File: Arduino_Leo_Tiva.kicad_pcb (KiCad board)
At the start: 4 copper layers, 68.6 x 52.1 mm, 53 parts, among them J1 USB_OTG, J10 Digital, J11 TDI, J12 TDO, J13 TXD, J14 RXD, J15 -AREF, J16 +AREF, J17 SPI 2 (D6,D7), J18 SERIAL 3, 4, J19 SERIAL 2, J2 TCK, J20 SPI 0, J21 SERIAL 1, J3 RST, J4 PF4, J5 ~HIB, J5V1 +5V, J6 TMS, J7 Power, J8 Analog, J9 Digital, SW1 RESET, U1 TM4C123GH6PM, U2 LM1117IMPX-3.3, Y1 32.768Khz, Y2 16MHz

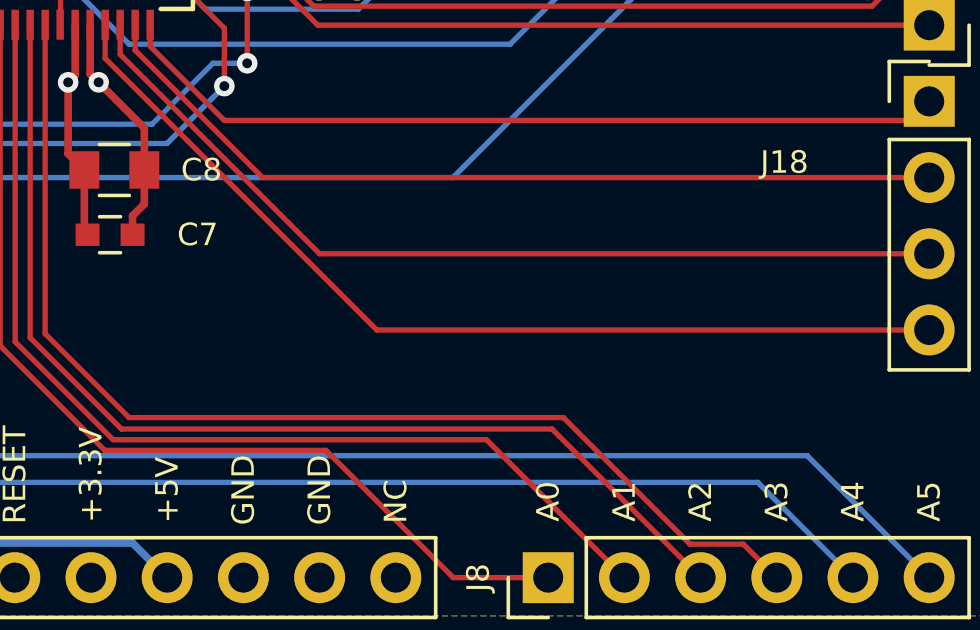
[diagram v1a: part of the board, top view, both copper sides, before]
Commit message: Added KiCAD silkscreen and name to top layer
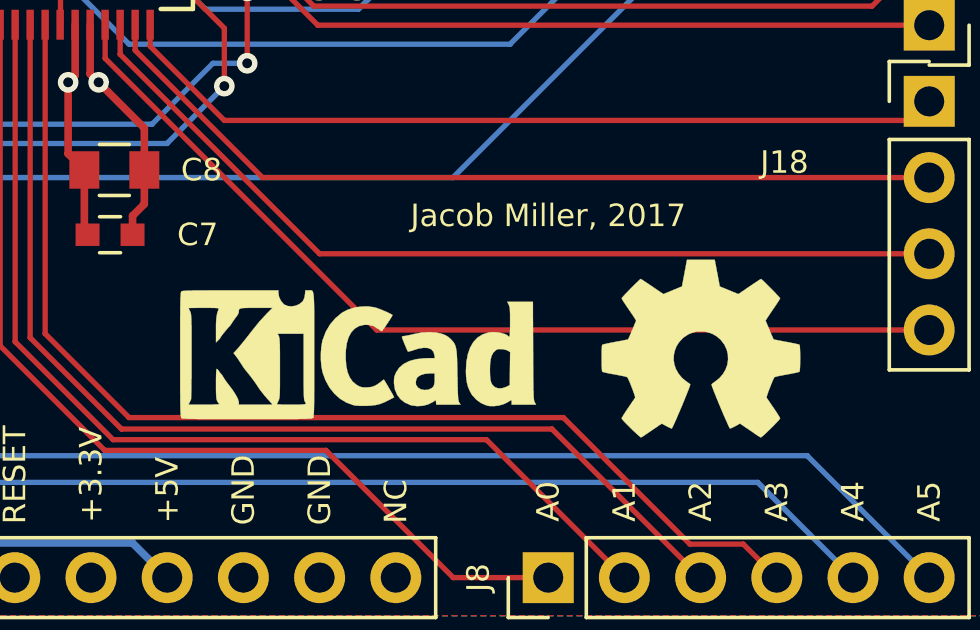
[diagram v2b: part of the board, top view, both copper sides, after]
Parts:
- added REF**: KiCAD Logo, Symbols:Symbol_KiCAD-Logo_CopperAndSilkScreenTop, F.Cu at (155.4, 116.2)
- added REF***: OSHW-Symbol_6.7x6mm_SilkScreen, Symbols:OSHW-Symbol_6.7x6mm_SilkScreen, F.Cu at (166.9, 116.2)
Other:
- board text added: "Jacob Miller, 2017"

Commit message: Fixed issue with incorrect schematic symbol and footprint for 3.3V regulator IC. Fixed typo in path
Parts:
- removed M** (x2): Lego-Hole-4.8mm, Custon-Mounting-Holes:Lego-Hole
- removed REF**: KiCAD Logo, Symbols:Symbol_KiCAD-Logo_CopperAndSilkScreenTop
- removed REF***: OSHW-Symbol_6.7x6mm_SilkScreen, Symbols:OSHW-Symbol_6.7x6mm_SilkScreen
- U2: value LM1117IMPX-3.3 -> LM1117-3.3; footprint TO_SOT_Packages_SMD_Local:SOT-223-3Lead_TabPin2 -> TO_SOT_Packages_SMD_Local:SOT-223
- turned U2 to 180 degrees
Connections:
- U2 pad 1: +5V -> GNDREF
- U2 pad 2: GNDREF -> +3V3
- U2 pad 3: +3V3 -> +5V
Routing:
- net GNDREF: track 92.7 -> 79.1 mm
- net +3V3: track 46.6 -> 52.0 mm
- net +5V: track 90.1 -> 92.2 mm
- net /PB6(MISO): track 19.6 -> 20.3 mm

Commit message: Fixed "Swap UART Labels on D0,D1 #7"
Had U0Tx and U0Rx labled incorrectly in schematic.
Fixed labels and rerouted signals to correct pins.
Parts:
- J3: value RST -> ~RST
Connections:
- U1 pad 17: /1(Tx) -> /0(Rx)
- U1 pad 18: /0(Rx) -> /1(Tx)
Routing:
- net /0(Rx): track 75.8 -> 71.6 mm, vias 2 -> 1
- net /PD7(U2TX): track 39.6 -> 42.3 mm, vias 2 -> 3
- net /1(Tx): track 68.5 -> 69.4 mm, vias 2 -> 1

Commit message: Modified LEGO mounting hole - Increased width by 0.05 mm - Removed through hole plating (now NPTH)
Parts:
- added P1: LEGO_Hole, Custom-Mounting-Holes:Lego-Hole, F.Cu at (116.0, 79.1)
- added P2: LEGO_Hole, Custom-Mounting-Holes:Lego-Hole, F.Cu at (116.0, 119.1)
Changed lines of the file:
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@@
   (general
     (links 134)
-    (no_connects 3)
+    (no_connects 1)
     (area 110.922999 73.584999 179.653001 125.805001)
     (thickness 1.6)
@@
     (tracks 631)
     (zones 0)
-    (modules 51)
+    (modules 53)
     (nets 59)
   )
@@
     )
   )
+  (module Custom-Mounting-Holes:Lego-Hole (layer Top)
+    (at 115.998 79.0956 90)
+    (tags "Lego, Hole")
+    (fp_text reference P1 (at 0 4 90) (layer F.SilkS)
+      (effects (font (size 0.75 0.75) (thickness 0.15)))
+    )
+    (fp_text value LEGO_Hole (at 0 -4 90) (layer F.Fab)
+      (effects (font (size 0.75 0.75) (thickness 0.15)))
+    )
+    (fp_line (start -4 -4) (end -3 -4) (layer Dwgs.User) (width 0.15))
+    (fp_line (start -4 -3) (end -4 -4) (layer Dwgs.User) (width 0.15))
+    (fp_line (start 4 4) (end 4 3) (layer Dwgs.User) (width 0.15))
+    (fp_line (start 3 4) (end 4 4) (layer Dwgs.User) (width 0.15))
+    (fp_line (start -4 4) (end -3 4) (layer Dwgs.User) (width 0.15))
+    (fp_line (start -4 3) (end -4 4) (layer Dwgs.User) (width 0.15))
+    (fp_line (start 4 -4) (end 3 -4) (layer Dwgs.User) (width 0.15))
+    (fp_line (start 4 -3) (end 4 -4) (layer Dwgs.User) (width 0.15))
+    (pad "" np_thru_hole circle (at 0 0 90) (size 6.05 6.05) (drill 4.8) (layers *.Cu *.Mask))
+  )
+  (module Custom-Mounting-Holes:Lego-Hole (layer Top)
+    (at 115.998 119.095 90)
+    (tags "Lego, Hole")
+    (fp_text reference P2 (at 0 4 90) (layer F.SilkS)
+      (effects (font (size 0.75 0.75) (thickness 0.15)))
+    )
+    (fp_text value LEGO_Hole (at 0 -4 90) (layer F.Fab)
+      (effects (font (size 0.75 0.75) (thickness 0.15)))
+    )
+    (fp_line (start -4 -4) (end -3 -4) (layer Dwgs.User) (width 0.15))
+    (fp_line (start -4 -3) (end -4 -4) (layer Dwgs.User) (width 0.15))
+    (fp_line (start 4 4) (end 4 3) (layer Dwgs.User) (width 0.15))
+    (fp_line (start 3 4) (end 4 4) (layer Dwgs.User) (width 0.15))
+    (fp_line (start -4 4) (end -3 4) (layer Dwgs.User) (width 0.15))
+    (fp_line (start -4 3) (end -4 4) (layer Dwgs.User) (width 0.15))
+    (fp_line (start 4 -4) (end 3 -4) (layer Dwgs.User) (width 0.15))
+    (fp_line (start 4 -3) (end 4 -4) (layer Dwgs.User) (width 0.15))
+    (pad "" np_thru_hole circle (at 0 0 90) (size 6.05 6.05) (drill 4.8) (layers *.Cu *.Mask))
+  )
   (gr_text "Jacob Miller, 2017" (at 161.798 111.76) (layer F.SilkS)

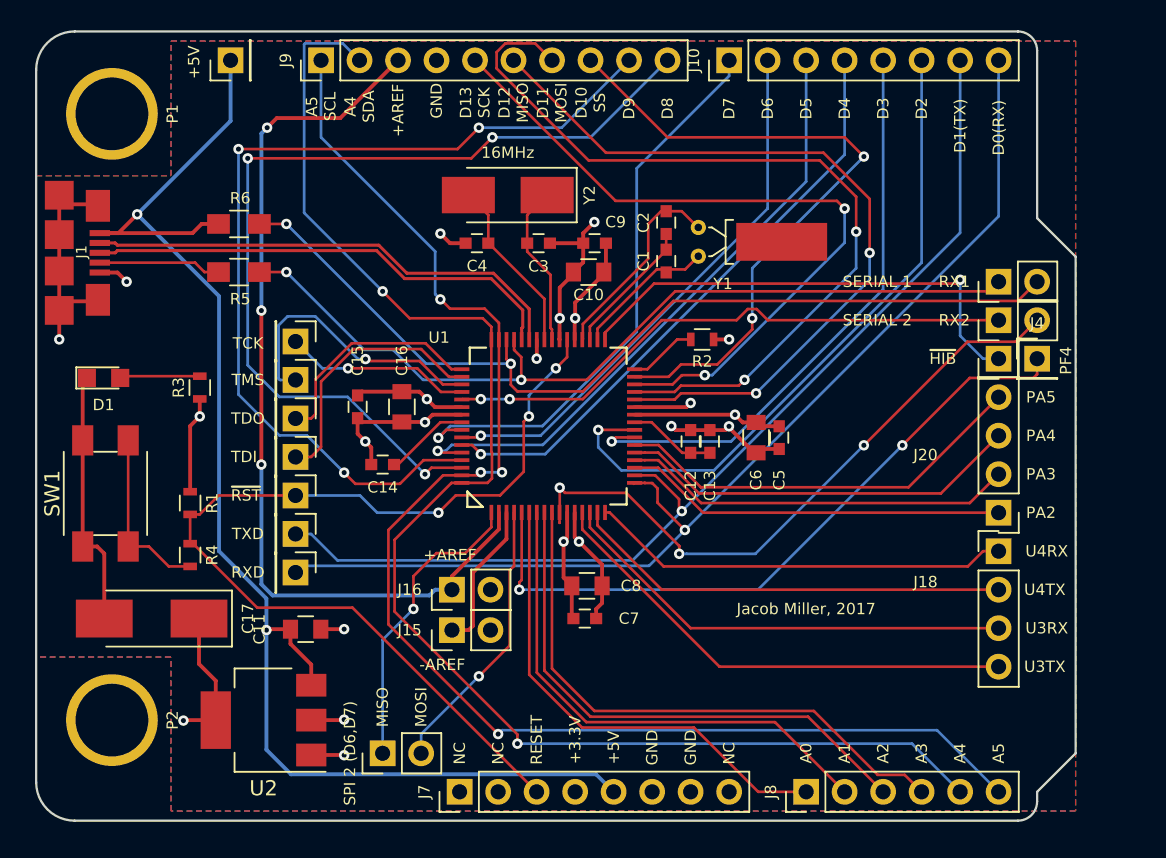
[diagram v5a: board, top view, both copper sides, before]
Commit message: Major changes to board layout and design leading towards revisoin v1.1
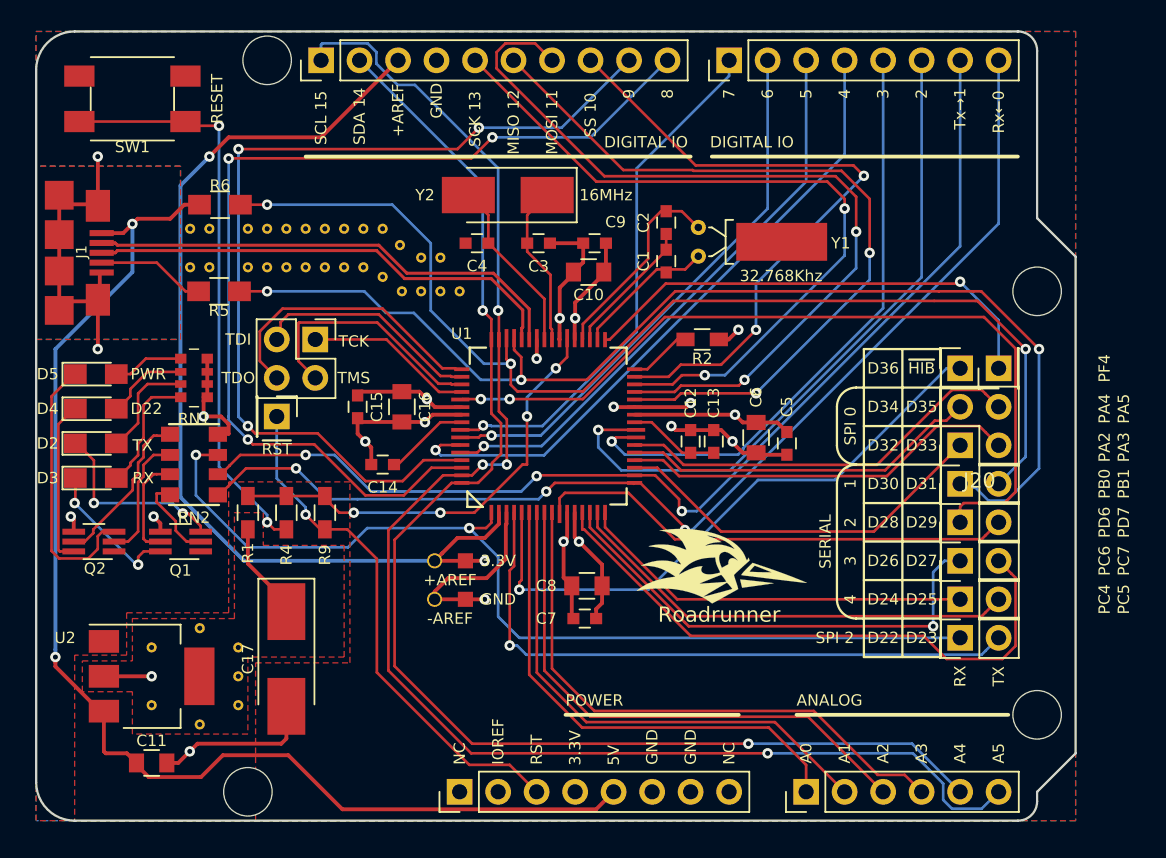
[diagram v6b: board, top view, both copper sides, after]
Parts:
- removed D1: Green, LEDs:LED_0805
- removed J11: TDI, Pin_Headers:Pin_Header_Straight_1x01_Pitch2.54mm
- removed J12: TDO, Pin_Headers:Pin_Header_Straight_1x01_Pitch2.54mm
- removed J18: SERIAL 3, 4, Socket_Strips:Socket_Strip_Straight_1x04_Pitch2.54mm
- removed J5V1: +5V, Pin_Headers:Pin_Header_Straight_1x01_Pitch2.54mm
- removed J6: TMS, Pin_Headers:Pin_Header_Straight_1x01_Pitch2.54mm
- removed P1, P2: LEGO_Hole, Custom-Mounting-Holes:Lego-Hole
- removed R3: 75, Resistors_SMD:R_0603
- added D2: Green, LEDs:LED_0805_HandSoldering, F.Cu at (114.9, 100.8)
- added D3: Green, LEDs:LED_0805_HandSoldering, F.Cu at (114.9, 103.1)
- added D4: Green, LEDs:LED_0805_HandSoldering, F.Cu at (114.9, 98.6)
- added D5: Green, LEDs:LED_0805_HandSoldering, F.Cu at (114.9, 96.3)
- added G***: LOGO, Custom-Mounting-Holes:My_Roadrunner, B.Cu at (123.7, 99.7)
- added G***: LOGO, Custom-Mounting-Holes:My_Roadrunner_smaller, F.Cu at (156.5, 109.0)
- added Q1: UM6K33N, TO_SOT_Packages_SMD_Local:SOT-363_SC-70-6_Handsoldering, F.Cu at (120.5, 107.3)
- added Q2: UM6K33N, TO_SOT_Packages_SMD_Local:SOT-363_SC-70-6_Handsoldering, F.Cu at (114.8, 107.3)
- added R9: 10k, Resistors_SMD:R_0603_HandSoldering, F.Cu at (130.0, 105.4)
- added REF**: VIA-0.33mm, Custom-Mounting-Holes:VIA-0.33mm, F.Cu at (124.3, 116.2)
- added REF**: VIA-0.33mm, Custom-Mounting-Holes:VIA-0.33mm, F.Cu at (121.2, 86.7)
- added REF**: VIA-0.33mm, Custom-Mounting-Holes:VIA-0.33mm, F.Cu at (122.4, 86.7)
- added REF**: VIA-0.33mm, Custom-Mounting-Holes:VIA-0.33mm, F.Cu at (125.0, 86.7)
- added REF**: VIA-0.33mm, Custom-Mounting-Holes:VIA-0.33mm, F.Cu at (126.2, 86.7)
- added REF**: VIA-0.33mm, Custom-Mounting-Holes:VIA-0.33mm, F.Cu at (127.5, 86.7)
- added REF**: VIA-0.33mm, Custom-Mounting-Holes:VIA-0.33mm, F.Cu at (125.0, 89.2)
- added REF**: VIA-0.33mm, Custom-Mounting-Holes:VIA-0.33mm, F.Cu at (126.2, 89.2)
- added REF**: VIA-0.33mm, Custom-Mounting-Holes:VIA-0.33mm, F.Cu at (127.5, 89.2)
- added REF**: VIA-0.33mm, Custom-Mounting-Holes:VIA-0.33mm, F.Cu at (128.8, 86.7)
- added REF**: VIA-0.33mm, Custom-Mounting-Holes:VIA-0.33mm, F.Cu at (128.8, 89.2)
- added REF**: VIA-0.33mm, Custom-Mounting-Holes:VIA-0.33mm, F.Cu at (124.3, 118.1)
- added REF**: VIA-0.33mm, Custom-Mounting-Holes:VIA-0.33mm, F.Cu at (130.0, 89.2)
- added REF**: VIA-0.33mm, Custom-Mounting-Holes:VIA-0.33mm, F.Cu at (131.3, 89.2)
- added REF**: VIA-0.33mm, Custom-Mounting-Holes:VIA-0.33mm, F.Cu at (138.9, 90.8)
- added REF**: VIA-0.33mm, Custom-Mounting-Holes:VIA-0.33mm, F.Cu at (137.7, 90.8)
- added REF**: VIA-0.33mm, Custom-Mounting-Holes:VIA-0.33mm, F.Cu at (136.4, 90.8)
- added REF**: VIA-0.33mm, Custom-Mounting-Holes:VIA-0.33mm, F.Cu at (135.1, 90.8)
- added REF**: VIA-0.33mm, Custom-Mounting-Holes:VIA-0.33mm, F.Cu at (133.9, 89.9)
- added REF**: VIA-0.33mm, Custom-Mounting-Holes:VIA-0.33mm, F.Cu at (132.6, 89.2)
- added REF**: VIA-0.33mm, Custom-Mounting-Holes:VIA-0.33mm, F.Cu at (137.7, 88.6)
- added REF**: VIA-0.33mm, Custom-Mounting-Holes:VIA-0.33mm, F.Cu at (136.4, 88.6)
- added REF**: VIA-0.33mm, Custom-Mounting-Holes:VIA-0.33mm, F.Cu at (124.3, 114.3)
- added REF**: VIA-0.33mm, Custom-Mounting-Holes:VIA-0.33mm, F.Cu at (135.0, 87.8)
- added REF**: VIA-0.33mm, Custom-Mounting-Holes:VIA-0.33mm, F.Cu at (133.9, 86.7)
- added REF**: VIA-0.33mm, Custom-Mounting-Holes:VIA-0.33mm, F.Cu at (132.6, 86.7)
- added REF**: VIA-0.33mm, Custom-Mounting-Holes:VIA-0.33mm, F.Cu at (131.3, 86.7)
- added REF**: VIA-0.33mm, Custom-Mounting-Holes:VIA-0.33mm, F.Cu at (130.0, 86.7)
- added REF**: VIA-0.33mm, Custom-Mounting-Holes:VIA-0.33mm, F.Cu at (121.8, 119.4)
- added REF**: VIA-0.33mm, Custom-Mounting-Holes:VIA-0.33mm, F.Cu at (121.8, 113.0)
- added REF**: VIA-0.33mm, Custom-Mounting-Holes:VIA-0.33mm, F.Cu at (118.6, 118.1)
- added REF**: VIA-0.33mm, Custom-Mounting-Holes:VIA-0.33mm, F.Cu at (118.6, 114.3)
- added REF**: VIA-0.33mm, Custom-Mounting-Holes:VIA-0.33mm, F.Cu at (122.4, 89.2)
- added REF**: VIA-0.33mm, Custom-Mounting-Holes:VIA-0.33mm, F.Cu at (121.2, 89.2)
- added REF***: KiCad-Logo2_12mm_SilkScreen, Symbols:KiCad-Logo2_12mm_SilkScreen, B.Cu at (164.3, 99.7)
- added REF***: OSHW-Logo2_9.8x8mm_SilkScreen, Symbols:OSHW-Logo2_9.8x8mm_SilkScreen, B.Cu at (144.8, 99.7)
- added RN1: 75, Project-Symbols_Local:YC164-JR-0775RL, F.Cu at (121.4, 96.5)
- added RN2: 10k, Project-Symbols_Local:CRA12E08310K0JTR, F.Cu at (121.4, 102.2)
- added T1: M_Hole, Custom-Mounting-Holes:ArduinoMountingHole_3.2mm, F.Cu at (125.0, 123.8)
- added T2: M_Hole, Custom-Mounting-Holes:ArduinoMountingHole_3.2mm, F.Cu at (177.0, 118.7)
- added T3: M_Hole, Custom-Mounting-Holes:ArduinoMountingHole_3.2mm, F.Cu at (126.2, 75.6)
- added T4: M_Hole, Custom-Mounting-Holes:ArduinoMountingHole_3.2mm, F.Cu at (177.0, 90.8)
- J13: value TXD -> SERIAL 4; footprint Pin_Headers:Pin_Header_Straight_1x01_Pitch2.54mm -> Socket_Strips:Socket_Strip_Straight_1x02_Pitch2.54mm
- J14: value RXD -> SERIAL 3; footprint Pin_Headers:Pin_Header_Straight_1x01_Pitch2.54mm -> Socket_Strips:Socket_Strip_Straight_1x02_Pitch2.54mm
- J15, J16: footprint Pin_Headers:Pin_Header_Straight_1x02_Pitch2.54mm -> Custom-Mounting-Holes:NetTie-I_Connected_SMD
- J17: value SPI 2 (D6,D7) -> SPI 2 (D22,D23)
- J2: value TCK -> JTAG; footprint Pin_Headers:Pin_Header_Straight_1x01_Pitch2.54mm -> Connectors_Local:Pin_Header_Straight_2x02_Pitch2.54mm
- J20: footprint Socket_Strips:Socket_Strip_Straight_1x04_Pitch2.54mm -> Socket_Strips:Socket_Strip_Straight_2x02_Pitch2.54mm
- J5: footprint Pin_Headers:Pin_Header_Straight_1x01_Pitch2.54mm -> Socket_Strips:Socket_Strip_Straight_1x01_Pitch2.54mm
- R1, R2, R4: footprint Resistors_SMD:R_0603 -> Resistors_SMD:R_0603_HandSoldering
- moved J13 44.1 mm to (172.0, 111.1), turned to 90 degrees
- moved J14 43.9 mm to (172.0, 108.6), turned to 90 degrees
- moved J17 38.9 mm to (172.0, 113.7)
- moved SW1 26.1 mm to (117.3, 78.1), turned to 0 degrees
- moved J19 13.6 mm to (172.0, 106.0)
- moved J21 13.6 mm to (172.0, 103.5)
- moved C11 13.5 mm to (118.6, 121.9)
- moved C17 9.28 mm to (127.5, 115.1), turned to 270 degrees
- moved U2 7.93 mm to (118.6, 116.2), turned to 0 degrees
- moved R4 6.94 mm to (127.5, 105.4)
- moved J3 5.36 mm to (126.9, 99.1)
- moved J4 5.12 mm to (172.0, 95.9)
- moved J20 5.12 mm to (172.0, 101.0)
- moved R1 3.86 mm to (125.0, 105.4), turned to 90 degrees
- moved J15 2.04 mm to (138.3, 111.1), turned to 0 degrees
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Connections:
- J10 pad 7: /1(Tx) -> /D1(TX)
- J10 pad 8: /0(Rx) -> /D0(RX)
- J13 pad 1: /1(Tx) -> /PC4(U4RX)
- J14 pad 1: /0(Rx) -> /PC6(U3RX)
- J3 pad 1: /RESET -> /~RST
- J7 pad 2: (no net) -> +3V3
- J7 pad 3: /RESET -> /~RST
- R1 pad 2: /RESET -> /~TARGET_RST
- R4 pad 1: /RESET -> /~TARGET_RST
- U1 pad 17: /0(Rx) -> /D0(RX)
- U1 pad 18: /1(Tx) -> /D1(TX)
- U1 pad 38: /RESET -> /~TARGET_RST
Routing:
- net /D0(RX): track 0.00 -> 74.1 mm, vias 0 -> 3
- net /D1(TX): track 0.00 -> 71.8 mm, vias 0 -> 3
- net /0(Rx): track 71.6 -> 0.00 mm, vias 1 -> 0
- net /1(Tx): track 69.4 -> 0.00 mm, vias 1 -> 0
- net /RESET: track 65.6 -> 0.00 mm, vias 3 -> 0
- net /PB6(MISO): track 20.3 -> 64.4 mm, vias 1 -> 2
- net /~RST: track 0.00 -> 34.7 mm, vias 0 -> 1
- net /~TARGET_RST: track 0.00 -> 29.7 mm, vias 0 -> 4
- net Net-(R4-Pad2): track 11.6 -> 38.6 mm, vias 0 -> 2
- net /PB7(MOSI): track 18.4 -> 41.9 mm
- net /PB0(U1RX): track 57.2 -> 76.4 mm, vias 2 -> 3
- net /Q2D2: track 0.00 -> 17.9 mm
- net /PD6(U2RX): track 38.2 -> 54.2 mm
- net /PB1(U1TX): track 61.4 -> 75.4 mm, vias 2 -> 3
- net /Q1D2: track 0.00 -> 12.6 mm, vias 0 -> 2
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- added copper zone on F.Cu, net +3V3
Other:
- board text added: "1"
- board text added: "2"
- board text added: "3"
- board text added: "3.3V"
- board text added: "4"
- board text added: "5"
- board text added: "5V"
- board text added: "6"
- board text added: "7"
- board text added: "8"
- board text added: "9"
- board text added: "ANALOG"
- board text added: "D22"
- board text added: "D23"
- board text added: "D24"
- board text added: "D25"
- board text added: "D26"
- board text added: "D27"
- board text added: "D28"
- board text added: "D29"
- board text added: "D30"
- board text added: "D31"
- board text added: "D32"
- board text added: "D33"
- board text added: "D34"
- board text added: "D35"
- board text added: "D36"
- board text added: "DIGITAL IO"
- board text added: "IOREF"
- board text added: "MISO 12"
- board text added: "MOSI 11"
- board text added: "PB0"
- board text added: "PB1"
- board text added: "PC4"
- board text added: "PC5"
- board text added: "PC6"
- board text added: "PC7"
- board text added: "PD6"
- board text added: "PD7"
- board text added: "PF4"
- board text added: "POWER"
- board text added: "PWR"
- board text added: "RST"
- board text added: "RX"
- board text added: "Roadrunner"
- board text added: "Roadrunner Rev 1.1 (Jacob Miller 2017)"
- board text added: "Rx←0"
- board text added: "SCK 13"
- board text added: "SCL 15"
- board text added: "SDA 14"
- board text added: "SERIAL"
- board text added: "SPI 0"
- board text added: "SPI 2"
- board text added: "SS 10"
- board text added: "TCK"
- board text added: "TDI"
- board text added: "TDO"
- board text added: "TMS"
- board text added: "TX"
- board text added: "Tx→1"
- board text added: "~HIB"
- board text removed: "+3.3V"
- board text removed: "+5V"
- board text removed: "A4 SDA"
- board text removed: "A5 SCL"
- board text removed: "D0(RX)"
- board text removed: "D1(TX)"
- board text removed: "D10 SS"
- board text removed: "D11 MOSI"
- board text removed: "D12 MISO"
- board text removed: "D13 SCK"
- board text removed: "D2"
- board text removed: "D3"
- board text removed: "D4"
- board text removed: "D5"
- board text removed: "D6"
- board text removed: "D7"
- board text removed: "D8"
- board text removed: "D9"
- board text removed: "Jacob Miller, 2017"
- board text removed: "MISO"
- board text removed: "MOSI"
- board text removed: "RESET"
- board text removed: "U3RX"
- board text removed: "U3TX"
- board text removed: "U4RX"
- board text removed: "U4TX"

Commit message: Recent modifications to layout. Switching to resistor arrays. Adding Roadrunner image.
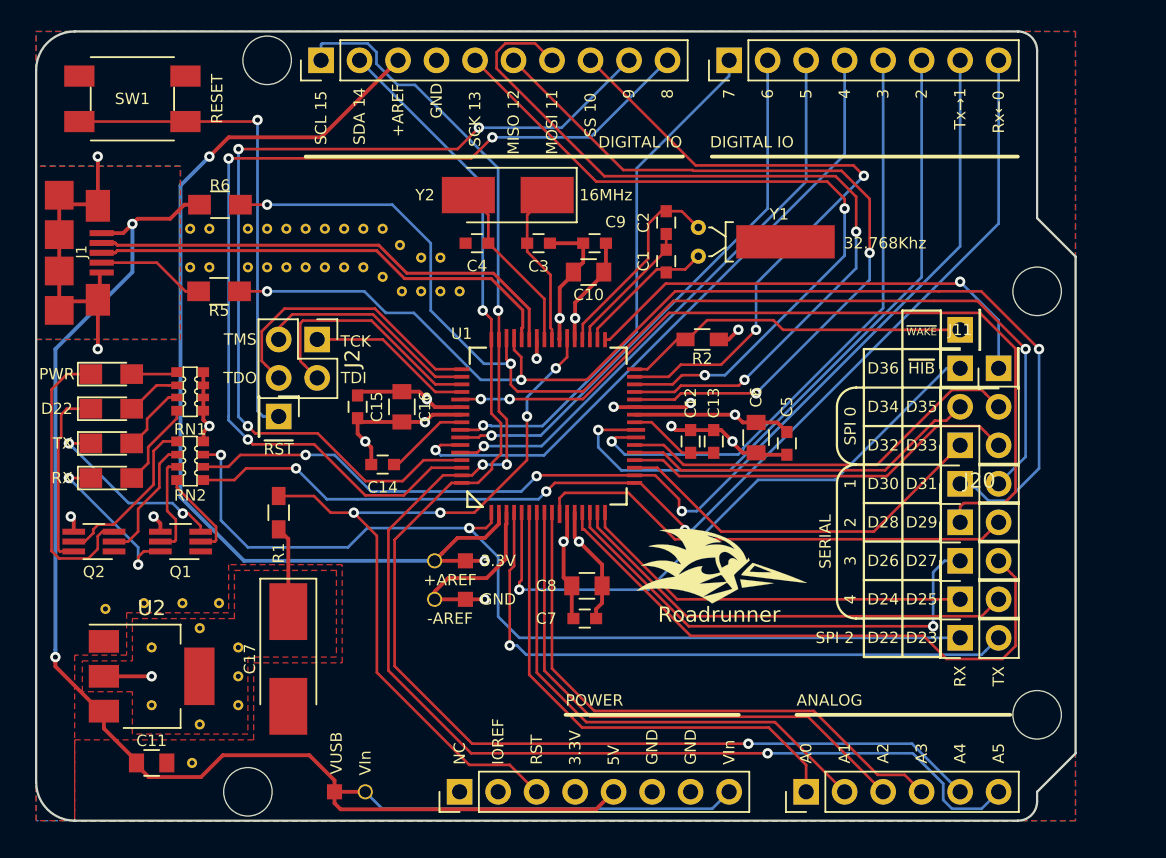
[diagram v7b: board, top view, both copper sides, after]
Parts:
- removed R4: 100, Resistors_SMD:R_0603_HandSoldering
- removed R9: 10k, Resistors_SMD:R_0603_HandSoldering
- added J11: ~WAKE, Socket_Strips:Socket_Strip_Straight_1x01_Pitch2.54mm, F.Cu at (172.0, 93.3)
- added J6: VIn, Custom-Mounting-Holes:NetTie-I_Connected_SMD, F.Cu at (131.7, 123.8)
- added REF**: VIA-0.33mm, Custom-Mounting-Holes:VIA-0.33mm, F.Cu at (120.7, 111.4)
- added REF**: VIA-0.33mm, Custom-Mounting-Holes:VIA-0.33mm, F.Cu at (115.6, 111.8)
- added REF**: VIA-0.33mm, Custom-Mounting-Holes:VIA-0.33mm, F.Cu at (118.1, 111.4)
- added REF**: VIA-0.33mm, Custom-Mounting-Holes:VIA-0.33mm, F.Cu at (123.1, 111.4)
- added REF**: VIA-0.33mm, Custom-Mounting-Holes:VIA-0.33mm, F.Cu at (121.3, 121.9)
- J2: footprint Connectors_Local:Pin_Header_Straight_2x02_Pitch2.54mm -> Pin_Headers:Pin_Header_Straight_2x02_Pitch2.54mm
- Q1, Q2: footprint TO_SOT_Packages_SMD_Local:SOT-363_SC-70-6_Handsoldering -> TO_SOT_Packages_SMD:SOT-363_SC-70-6_Handsoldering
- RN2: footprint Project-Symbols_Local:CRA12E08310K0JTR -> Project-Symbols_Local:YC164-JR-0775RL
- U2: footprint TO_SOT_Packages_SMD_Local:SOT-223 -> TO_SOT_Packages_SMD:SOT-223
- Y1: footprint Crystals_Local:Crystal_DS26_d2.0mm_l6.0mm_Horizontal_1EP_style1 -> Project-Symbols_Local:Crystal_C26-LF_d2.1mm_l6.5mm_Horizontal_1EP_style1
- moved R1 2.03 mm to (127.0, 105.4)
- moved J2 1.89 mm to (129.5, 94.0)
- moved D2 1.02 mm to (116.0, 100.8)
- moved D3 1.02 mm to (116.0, 103.1)
- moved D4 1.02 mm to (116.0, 98.6)
- moved D5 1.02 mm to (116.0, 96.3)
- moved RN1 0.92 mm to (121.2, 97.4)
- moved RN2 0.36 mm to (121.2, 102.0)
- moved C17 0.13 mm to (127.6, 115.1)
- moved J3 0.13 mm to (127.0, 99.1)
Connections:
- net Net-(C1-Pad1) renamed /XOSC0
- net Net-(C2-Pad2) renamed /XOSC1
- net Net-(C3-Pad1) renamed /OCS0
- net Net-(C4-Pad1) renamed /OCS1
- J7 pad 8: (no net) -> /VIn
- R1 pad 2: /~TARGET_RST -> /~RST
- SW1 pad 2: Net-(R4-Pad2) -> /~RST
- U1 pad 38: /~TARGET_RST -> /~RST
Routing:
- net /~RST: track 34.7 -> 85.5 mm, vias 1 -> 5
- net Net-(R4-Pad2): track 38.6 -> 0.00 mm, vias 2 -> 0
- net /~TARGET_RST: track 29.7 -> 0.00 mm, vias 4 -> 0
- net /VIn: track 0.00 -> 24.9 mm
- net /~WAKE: track 4.52 -> 23.4 mm
- net GNDREF: track 76.0 -> 65.4 mm, vias 14 -> 13
- net +3V3: track 54.4 -> 51.3 mm
- net /RX_LED: track 8.38 -> 5.73 mm
- net /TX_LED: track 7.12 -> 4.65 mm
- net /PB6_LED: track 5.54 -> 3.62 mm
- net /PWR_LED: track 4.67 -> 3.04 mm
- net /Q1D1: track 9.67 -> 11.3 mm
- net /Q2D2: track 17.9 -> 19.2 mm
- net /Q2D1: track 10.9 -> 12.2 mm
- net /PB6(MISO): track 64.4 -> 63.4 mm
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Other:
- board text added: "PB6"
- board text added: "PB7"
- board text added: "VIn"
- board text added: "VUSB"
- board text added: "~WAKE"
